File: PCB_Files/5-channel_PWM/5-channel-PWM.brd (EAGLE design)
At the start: 58 x 63 mm, 28 parts, among them Q1 N-MOS, Q2 N-MOS, Q3 N-MOS, Q4 N-MOS, Q5 N-MOS

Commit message: fixed design
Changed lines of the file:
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@@
 <setting verticaltext="up"/>
 </settings>
-<grid distance="1" unitdist="mm" unit="mm" style="lines" multiple="1" display="yes" altdistance="1" altunitdist="mm" altunit="mm"/>
+<grid distance="12.5" unitdist="mil" unit="mil" style="lines" multiple="1" display="yes" altdistance="1" altunitdist="mm" altunit="mm"/>
 <layers>
 <layer number="1" name="Top" color="4" fill="1" visible="yes" active="yes"/>
@@
 </element>
 <element name="R1" library="diyHue" package="MULTI_RESISTOR" value="4k7" x="30.48" y="21.59" smashed="yes">
-<attribute name="VALUE" x="28.8544" y="21.1074" size="0.9906" layer="21" ratio="10"/>
+<attribute name="VALUE" x="29.21" y="22.86" size="0.9906" layer="21" ratio="10"/>
 </element>
 <element name="H1" library="holes" package="3,0-PAD" value="MOUNT-PAD-ROUND3.0" x="5" y="5"/>
@@
 <element name="H4" library="holes" package="3,0-PAD" value="MOUNT-PAD-ROUND3.0" x="5" y="58"/>
 <element name="BTN3" library="schalter_taster" package="KSM611A" value="" x="52.705" y="19.3675" rot="R180"/>
-<element name="R4" library="diyHue" package="MULTI_RESISTOR" value="4k7" x="30.48" y="16.51" smashed="yes">
-<attribute name="VALUE" x="28.8544" y="16.0274" size="0.9906" layer="21" ratio="10"/>
-</element>
+<element name="R4" library="diyHue" package="MULTI_RESISTOR" value="4k7" x="30.48" y="16.51" smashed="yes"/>
 <element name="Q1" library="transistor-fet" package="TO220" value="N-MOS" x="6.35" y="38.1"/>
 <element name="Q2" library="transistor-fet" package="TO220" value="N-MOS" x="17.78" y="38.1"/>
@@
 <attribute name="VALUE" x="16.5576" y="54.0258" size="1.27" layer="27" ratio="10"/>
 </element>
-<element name="R3" library="diyHue" package="MULTI_RESISTOR" value="4k7" x="40.005" y="13.97" smashed="yes" rot="R180">
-<attribute name="VALUE" x="41.6306" y="14.4526" size="0.9906" layer="21" ratio="10" rot="R180"/>
-</element>
-<element name="R6" library="diyHue" package="MULTI_RESISTOR" value="4k7" x="40.005" y="16.51" smashed="yes" rot="R180">
-<attribute name="VALUE" x="41.6306" y="16.9926" size="0.9906" layer="21" ratio="10" rot="R180"/>
-</element>
-<element name="R7" library="diyHue" package="MULTI_RESISTOR" value="4k7" x="40.005" y="19.05" smashed="yes" rot="R180">
-<attribute name="VALUE" x="41.6306" y="19.5326" size="0.9906" layer="21" ratio="10" rot="R180"/>
-</element>
-<element name="R8" library="diyHue" package="MULTI_RESISTOR" value="4k7" x="40.005" y="21.59" smashed="yes" rot="R180">
-<attribute name="VALUE" x="41.6306" y="22.0726" size="0.9906" layer="21" ratio="10" rot="R180"/>
-</element>
+<element name="R3" library="diyHue" package="MULTI_RESISTOR" value="4k7" x="40.005" y="13.97" smashed="yes" rot="R180"/>
+<element name="R6" library="diyHue" package="MULTI_RESISTOR" value="4k7" x="40.005" y="16.51" smashed="yes" rot="R180"/>
+<element name="R7" library="diyHue" package="MULTI_RESISTOR" value="4k7" x="40.005" y="19.05" smashed="yes" rot="R180"/>
+<element name="R8" library="diyHue" package="MULTI_RESISTOR" value="4k7" x="40.005" y="21.59" smashed="yes" rot="R180"/>
 <element name="R9" library="diyHue" package="MULTI_RESISTOR" value="4k7" x="40.005" y="24.13" smashed="yes" rot="R180">
-<attribute name="VALUE" x="41.6306" y="24.6126" size="0.9906" layer="21" ratio="10" rot="R180"/>
+<attribute name="VALUE" x="41.5925" y="26.3525" size="0.9906" layer="21" ratio="10" rot="R180"/>
 </element>
 <element name="BTN4" library="schalter_taster" package="KSM611A" value="" x="52.705" y="12.065" rot="R180"/>
-<element name="R5" library="diyHue" package="MULTI_RESISTOR" value="4k7" x="30.48" y="13.97" smashed="yes">
-<attribute name="VALUE" x="28.8544" y="13.4874" size="0.9906" layer="21" ratio="10"/>
-</element>
+<element name="R5" library="diyHue" package="MULTI_RESISTOR" value="4k7" x="30.48" y="13.97" smashed="yes"/>
 <element name="JP1" library="pinhead-2" package="1X06-S" value="" x="29.21" y="60.96" smashed="yes">
 <attribute name="VALUE" x="21.59" y="57.785" size="1.27" layer="27"/>
@@
 <element name="U$1" library="diyHue" package="BUCK_CONVERTER_TE818" value="BUCK_CONVERTER_TE818" x="15.24" y="19.05" rot="R270"/>
 <element name="BTN2" library="schalter_taster" package="KSM611A" value="" x="52.705" y="26.3525" rot="R180"/>
-<element name="R2" library="diyHue" package="MULTI_RESISTOR" value="4k7" x="30.48" y="19.05"/>
+<element name="R2" library="diyHue" package="MULTI_RESISTOR" value="4k7" x="30.48" y="19.05" smashed="yes"/>
 </elements>
 <signals>

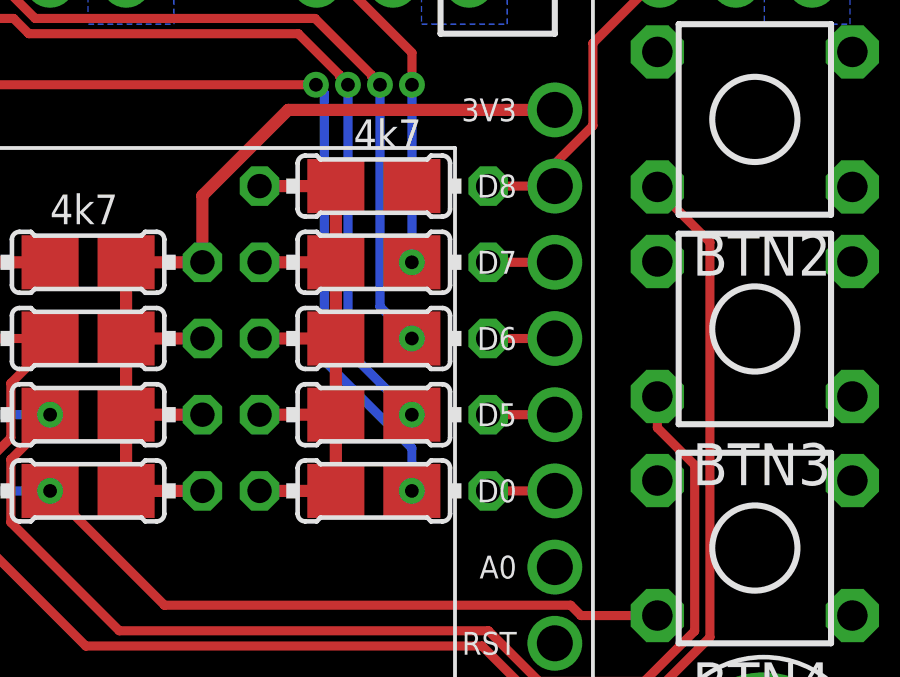
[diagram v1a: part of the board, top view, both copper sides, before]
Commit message: Updated gerber Files to fix breaking bug
the original design had some errors that were only found after they were ordered. Those bugs hab been fixed.
Also there were new pictures exported of the design and schematic
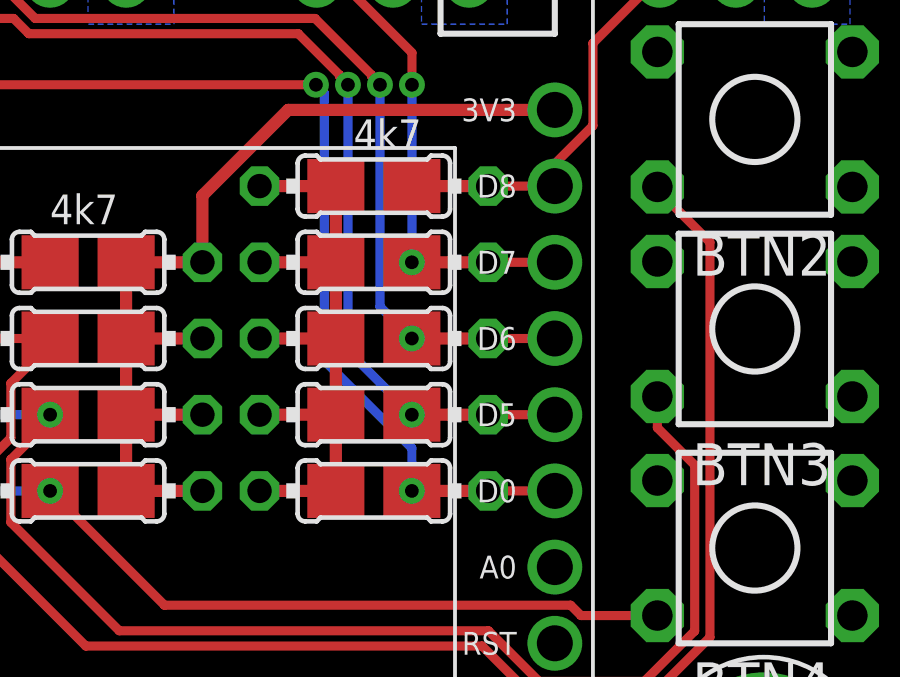
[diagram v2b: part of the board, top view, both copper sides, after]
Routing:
- net PWM_4: track 13.7 -> 16.2 mm
- net PWM_5: track 11.3 -> 13.8 mm
- net PWM_3: track 26.4 -> 29.0 mm
- net PWM_2: track 39.8 -> 42.3 mm
- net PWM_1: track 54.8 -> 57.4 mm
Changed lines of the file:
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@@
 <?xml version="1.0" encoding="utf-8"?>
 <!DOCTYPE eagle SYSTEM "eagle.dtd">
-<eagle version="9.1.3">
+<eagle version="6.6.0">
 <drawing>
 <settings>
 <setting alwaysvectorfont="yes"/>
-<setting keepoldvectorfont="yes"/>
 <setting verticaltext="up"/>
 </settings>
@@
 <param name="dpMaxLengthDifference" value="10mm"/>
 <param name="dpGapFactor" value="2.5"/>
+<param name="checkGrid" value="0"/>
 <param name="checkAngle" value="0"/>
 <param name="checkFont" value="1"/>
 <param name="checkRestrict" value="1"/>
-<param name="checkStop" value="0"/>
-<param name="checkValues" value="0"/>
-<param name="checkNames" value="1"/>
-<param name="checkWireStubs" value="1"/>
-<param name="checkPolygonWidth" value="0"/>
 <param name="useDiameter" value="13"/>
 <param name="maxErrors" value="50"/>
@@
 <pass name="Default">
 <param name="RoutingGrid" value="50mil"/>
-<param name="AutoGrid" value="1"/>
-<param name="Efforts" value="0"/>
-<param name="TopRouterVariant" value="1"/>
 <param name="tpViaShape" value="round"/>
 <param name="PrefDir.1" value="*"/>
@@
 <wire x1="9.525" y1="26.46013125" x2="9.09986875" y2="26.46013125" width="0.3048" layer="1"/>
 <wire x1="9.09986875" y1="26.46013125" x2="3.81" y2="31.75" width="0.3048" layer="1"/>
-<wire x1="41.271425" y1="13.97" x2="43.815" y2="13.97" width="0" layer="19" extent="1-1"/>
+<wire x1="41.271425" y1="13.97" x2="43.815" y2="13.97" width="0.4064" layer="1"/>
 </signal>
 <signal name="PWM_2">
@@
 <wire x1="37.48635625" y1="29.21" x2="28.50508125" y2="29.21" width="0.3048" layer="1"/>
 <wire x1="27.99708125" y1="29.718" x2="17.28550625" y2="29.718" width="0.3048" layer="1"/>
-<wire x1="41.271425" y1="16.51" x2="43.815" y2="16.51" width="0" layer="19" extent="1-1"/>
+<wire x1="41.271425" y1="16.51" x2="43.815" y2="16.51" width="0.4064" layer="1"/>
 </signal>
 <signal name="PWM_3">
@@
 <wire x1="39.9288" y1="27.83435625" x2="38.04515625" y2="29.718" width="0.3048" layer="1"/>
 <wire x1="38.04515625" y1="29.718" x2="28.71550625" y2="29.718" width="0.3048" layer="1"/>
-<wire x1="41.271425" y1="19.05" x2="43.815" y2="19.05" width="0" layer="19" extent="1-1"/>
+<wire x1="41.271425" y1="19.05" x2="43.815" y2="19.05" width="0.4064" layer="1"/>
 </signal>
 <signal name="PWM_4">
@@
 <wire x1="41.275" y1="27.5082" x2="41.275" y2="28.575" width="0.3048" layer="1"/>
 <wire x1="41.275" y1="28.575" x2="38.1" y2="31.75" width="0.3048" layer="1"/>
-<wire x1="41.271425" y1="21.59" x2="43.815" y2="21.59" width="0" layer="19" extent="1-1"/>
+<wire x1="41.271425" y1="21.59" x2="43.815" y2="21.59" width="0.4064" layer="1"/>
 </signal>
 <signal name="PWM_5">
@@
 <wire x1="47.3075" y1="26.14394375" x2="47.3075" y2="28.8925" width="0.3048" layer="1"/>
 <wire x1="49.53" y1="31.115" x2="49.53" y2="31.75" width="0.3048" layer="1"/>
-<wire x1="41.271425" y1="24.13" x2="43.815" y2="24.13" width="0" layer="19" extent="1-1"/>
+<wire x1="41.271425" y1="24.13" x2="43.815" y2="24.13" width="0.4064" layer="1"/>
 </signal>
 <signal name="N$1">
@@
 </signal>
 </signals>
-<mfgpreviewcolors>
-<mfgpreviewcolor name="soldermaskcolor" color="0xC8008000"/>
-<mfgpreviewcolor name="silkscreencolor" color="0xFFFEFEFE"/>
-<mfgpreviewcolor name="backgroundcolor" color="0xFF282828"/>
-<mfgpreviewcolor name="coppercolor" color="0xFFFFBF00"/>
-<mfgpreviewcolor name="substratecolor" color="0xFF786E46"/>
-</mfgpreviewcolors>
 <errors>
 </errors>
